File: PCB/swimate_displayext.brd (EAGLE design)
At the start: 50.9 x 51.2 mm, 56 parts, among them IC1 LPC11U24, T1 BSS84, T2 BSS84, U1 USD-SOCKETNEW, U3 NC7SV86P5X, U5 DS3231MZ/V+T, U6 MAX1595EUA33+, U7 MAX1811ESA-T, U8 MAX16054AZT+T, U9 HC_05, Y1 12.000MHz

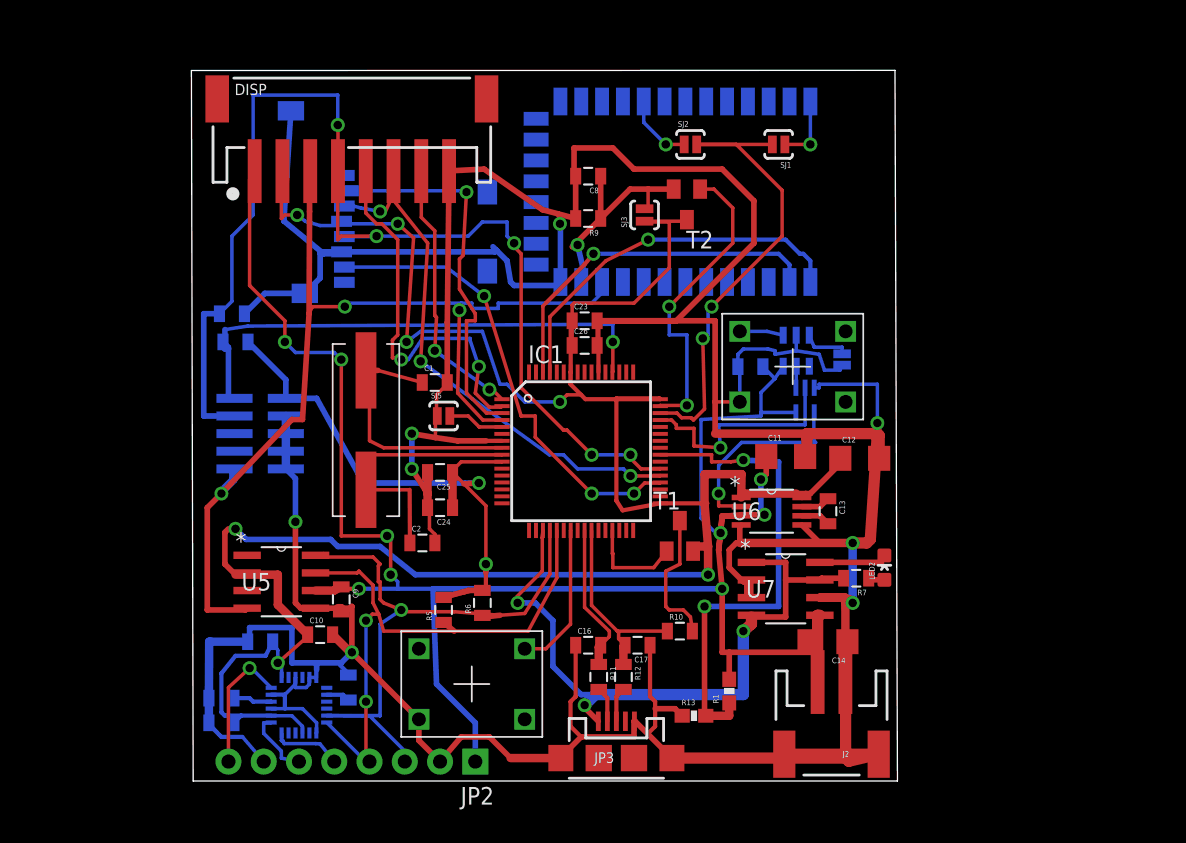
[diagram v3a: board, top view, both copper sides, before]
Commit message: Displayboard completed.. Need to check connector width
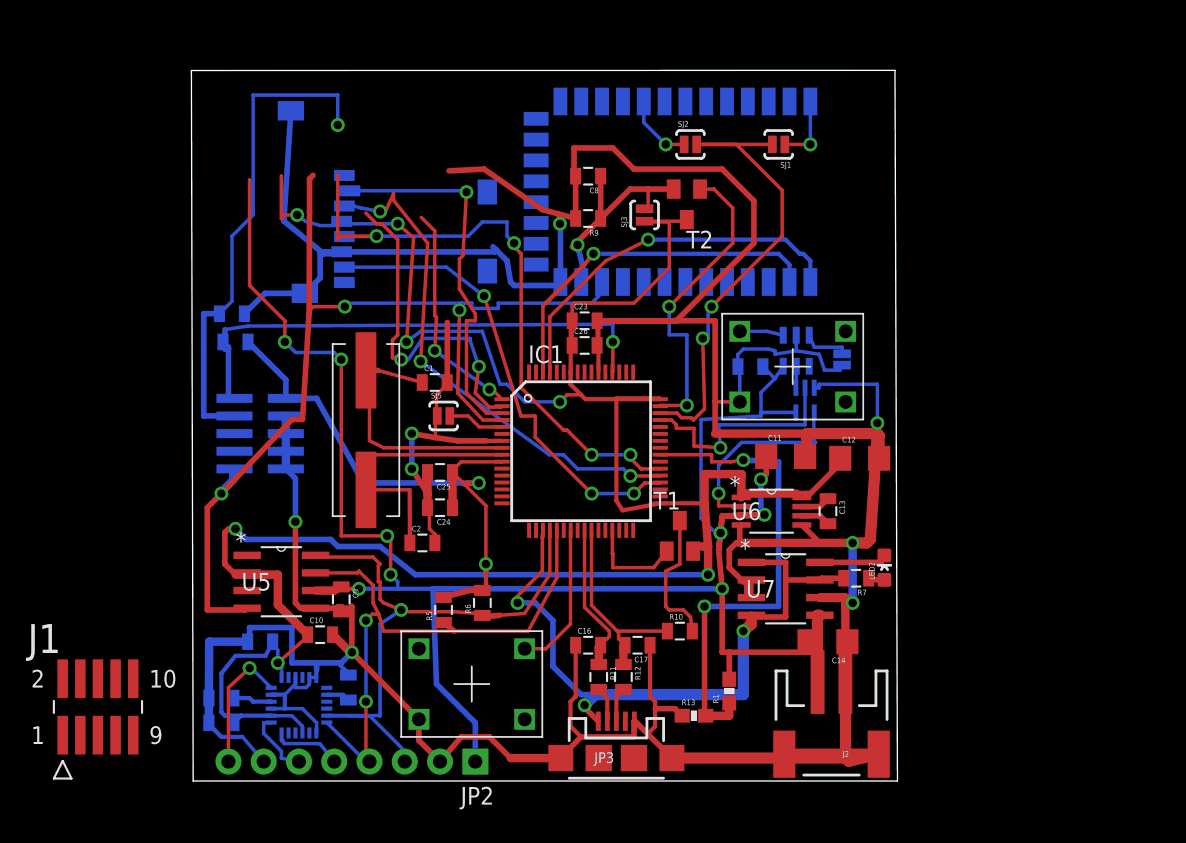
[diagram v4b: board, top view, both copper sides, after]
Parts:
- removed DISP: (no value), microbuilder:JSTPH8
- added J1: FTSH-105-01-L-DV, SAMTEC-HTSW-FTxx_By_element14_Batch_1:SAMTEC_FTSH-105-01-L-DV
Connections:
- net 3.3V: now also J1.2; no longer DISP.2
- net DISP_CS: now also J1.7; no longer DISP.5
- net DISP_DC: now also J1.1; no longer DISP.7
- net GND: now also J1.10, J1.6, J1.8; no longer DISP.8
- net RST: now also J1.3; no longer DISP.3
- net SPI0_MOSI: now also J1.9; no longer DISP.6
- net SPI0_SCK: now also J1.5; no longer DISP.4
- net VBAT: now also J1.4; no longer DISP.1
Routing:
- net GND: track 386.1 -> 375.2 mm
- net DISP_DC: track 19.4 -> 16.1 mm
- net SPI0_SCK: track 84.0 -> 80.8 mm
- net DISP_CS: track 27.7 -> 24.6 mm
- net SPI0_MOSI: track 39.2 -> 37.5 mm
- net VBAT: track 139.0 -> 138.3 mm
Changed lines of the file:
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@@
 <element name="R1" library="SparkFun-Passives" package="0603-RES" value="10k" x="38.608" y="6.096" rot="R90"/>
 <element name="R13" library="SparkFun-Passives" package="0603-RES" value="24k" x="36.068" y="4.318"/>
-<element name="DISP" library="microbuilder" package="JSTPH8" value="" x="11.43" y="47.244"/>
 <element name="SJ4" library="SparkFun-Passives" package="SJ_2S-NOTRACE" value="SOLDERJUMPERNC2" x="46.736" y="29.972" rot="MR90"/>
 <element name="U3" library="Fairchild_By_element14_Batch_1" package="SOT65P210X110-5N" value="NC7SV86P5X" x="44.069" y="27.051" rot="MR270">
@@
 <attribute name="SUPPLIER" value="Fairchild Semiconductor" x="44.069" y="27.051" size="1.778" layer="28" rot="MR270" display="off"/>
 <attribute name="OC_FARNELL" value="1467343" x="44.069" y="27.051" size="1.778" layer="28" rot="MR270" display="off"/>
+</element>
+<element name="J1" library="SAMTEC-HTSW-FTxx_By_element14_Batch_1" package="SAMTEC_FTSH-105-01-L-DV" value="FTSH-105-01-L-DV" x="-6.858" y="4.953">
+<attribute name="PACKAGE" value="HEADER, 1.27MM, 2X5WAY, SMT" x="-6.858" y="4.953" size="1.778" layer="27" display="off"/>
+<attribute name="OC_NEWARK" value="11P4814" x="-6.858" y="4.953" size="1.778" layer="27" display="off"/>
+<attribute name="MPN" value="FTSH-105-01-L-DV" x="-6.858" y="4.953" size="1.778" layer="27" display="off"/>
+<attribute name="SUPPLIER" value="SAMTEC" x="-6.858" y="4.953" size="1.778" layer="27" display="off"/>
+<attribute name="OC_FARNELL" value="1667759" x="-6.858" y="4.953" size="1.778" layer="27" display="off"/>
 </element>
 </elements>
@@
 <contactref element="U6" pad="3"/>
 <contactref element="R1" pad="2"/>
-<contactref element="DISP" pad="1"/>
 <wire x1="10.668" y1="13.6" x2="10.149" y2="13.335" width="0.6096" layer="1"/>
 <wire x1="10.149" y1="13.335" x2="8.8138" y2="13.335" width="0.6096" layer="1"/>
@@
 <wire x1="44.32" y1="9.652" x2="44.974" y2="8.89" width="0.3048" layer="1"/>
 <wire x1="38.608" y1="6.946" x2="38.608" y2="8.89" width="0.4064" layer="1"/>
-<wire x1="4.43" y1="43.544" x2="4.064" y2="42.924" width="0.254" layer="1"/>
 <wire x1="4.064" y1="42.924" x2="4.064" y2="35.306" width="0.254" layer="1"/>
 <wire x1="4.064" y1="35.306" x2="6.604" y2="32.766" width="0.254" layer="1"/>
@@
 <contactref element="U3" pad="5"/>
 <wire x1="43.4086" y1="26.162" x2="40.894" y2="26.162" width="0.254" layer="16"/>
+<contactref element="J1" pad="4"/>
+<wire x1="-8.128" y1="6.985" x2="8.8138" y2="13.335" width="0" layer="19" extent="1-1"/>
 </signal>
 <signal name="GND">
@@
 <contactref element="C17" pad="1"/>
 <contactref element="SW_MODE" pad="P$2"/>
-<contactref element="DISP" pad="8"/>
 <contactref element="U2" pad="1"/>
 <contactref element="U2" pad="11"/>
@@
 <wire x1="7.366" y1="21.408" x2="6.676" y2="22.098" width="0.4064" layer="16"/>
 <wire x1="18.299" y1="28.321" x2="18.303" y2="32.643" width="0.4064" layer="1"/>
-<wire x1="18.303" y1="32.643" x2="18.43" y2="43.544" width="0.4064" layer="1"/>
-<wire x1="18.43" y1="43.561" x2="18.43" y2="43.544" width="0.4064" layer="1"/>
 <wire x1="3.694" y1="33.274" x2="5.16" y2="34.74" width="0.4064" layer="16"/>
 <wire x1="5.16" y1="34.74" x2="8.04" y2="34.74" width="0.4064" layer="16"/>
@@
 <wire x1="26.416" y1="39.751" x2="26.416" y2="40.329078125" width="0.4064" layer="1"/>
 <wire x1="26.416" y1="40.329078125" x2="26.277096875" y2="40.46798125" width="0.4064" layer="1"/>
+<contactref element="J1" pad="6"/>
+<contactref element="J1" pad="8"/>
+<contactref element="J1" pad="10"/>
 <wire x1="29.094" y1="32.766" x2="28.956" y2="32.766" width="0" layer="19" extent="1-1"/>
+<wire x1="18.303" y1="32.643" x2="22.86" y2="35.56" width="0" layer="19" extent="1-16"/>
+<wire x1="-4.318" y1="6.985" x2="1.132" y2="5.588" width="0" layer="19" extent="1-16"/>
+<wire x1="-5.588" y1="6.985" x2="-4.318" y2="6.985" width="0" layer="19" extent="1-1"/>
+<wire x1="-6.858" y1="6.985" x2="-5.588" y2="6.985" width="0" layer="19" extent="1-1"/>
 </signal>
 <signal name="3.3V">
@@
 <contactref element="SJ3" pad="1"/>
 <contactref element="T1" pad="2"/>
-<contactref element="DISP" pad="2"/>
 <contactref element="U2" pad="3"/>
 <contactref element="U2" pad="13"/>
@@
 <wire x1="26.416" y1="26.924" x2="26.924" y2="27.432" width="0.254" layer="1"/>
 <wire x1="26.924" y1="27.432" x2="27.94" y2="27.432" width="0.254" layer="1"/>
-<wire x1="6.43" y1="43.544" x2="6.35" y2="43.21" width="0.254" layer="1"/>
 <wire x1="6.35" y1="43.21" x2="6.35" y2="40.132" width="0.254" layer="1"/>
 <wire x1="6.35" y1="40.132" x2="6.604" y2="40.386" width="0.254" layer="1"/>
@@
 <wire x1="6.37" y1="7.08" x2="6.37" y2="8.108" width="0.254" layer="16"/>
 <wire x1="6.37" y1="8.108" x2="6.096" y2="8.128" width="0.254" layer="16"/>
+<contactref element="J1" pad="2"/>
+<wire x1="-9.398" y1="6.985" x2="2.032" y2="7.366" width="0" layer="19" extent="1-16"/>
 </signal>
 <signal name="VUSB">
@@
 <contactref element="U1" pad="3"/>
 <contactref element="IC1" pad="37"/>
-<contactref element="DISP" pad="6"/>
-<wire x1="14.43" y1="43.544" x2="14.43" y2="41.91" width="0.254" layer="1"/>
 <wire x1="14.43" y1="41.91" x2="14.43" y2="41.45" width="0.254" layer="1"/>
 <wire x1="14.43" y1="41.45" x2="16.891" y2="38.354" width="0.254" layer="1"/>
@@
 <wire x1="13.462" y1="40.64" x2="13.795" y2="40.513" width="0.254" layer="1"/>
 <wire x1="13.795" y1="40.513" x2="14.43" y2="41.91" width="0.254" layer="1"/>
+<contactref element="J1" pad="9"/>
+<wire x1="-4.318" y1="2.921" x2="16.383" y2="29.845" width="0" layer="19" extent="1-1"/>
 </signal>
 <signal name="SPI0_SCK">
 <contactref element="U1" pad="5"/>
-<contactref element="DISP" pad="4"/>
 <contactref element="IC1" pad="38"/>
 <contactref element="JTAG1" pad="4"/>
@@
 <via x="10.414" y="46.863" extent="1-16" drill="0.6096"/>
 <wire x1="10.414" y1="46.863" x2="10.43" y2="46.466" width="0.254" layer="1"/>
-<wire x1="10.43" y1="46.466" x2="10.43" y2="43.544" width="0.254" layer="1"/>
-<wire x1="10.43" y1="43.544" x2="10.414" y2="43.274" width="0.254" layer="1"/>
 <wire x1="10.414" y1="43.274" x2="10.414" y2="38.608" width="0.254" layer="1"/>
 <wire x1="10.414" y1="38.608" x2="10.668" y2="38.862" width="0.254" layer="1"/>
@@
 <wire x1="32.258" y1="22.098" x2="33.62" y2="22.098" width="0.254" layer="1"/>
 <wire x1="33.62" y1="22.098" x2="33.64" y2="22.118" width="0.254" layer="1"/>
+<contactref element="J1" pad="5"/>
+<wire x1="10.43" y1="46.466" x2="10.414" y2="43.274" width="0" layer="19" extent="1-1"/>
+<wire x1="-6.858" y1="2.921" x2="0.762" y2="25.908" width="0" layer="19" extent="1-16"/>
 </signal>
 <signal name="SPI0_MISO">
@@
 <contactref element="JTAG1" pad="10"/>
 <contactref element="U9" pad="11"/>
-<contactref element="DISP" pad="3"/>
 <wire x1="3.8862" y1="12.065" x2="3.7592" y2="11.938" width="0.4064" layer="1"/>
 <wire x1="3.7592" y1="11.938" x2="1.016" y2="11.938" width="0.4064" layer="1"/>
@@
 <wire x1="2.032" y1="20.32" x2="7.112" y2="25.654" width="0.4064" layer="1"/>
 <wire x1="7.112" y1="25.654" x2="7.874" y2="25.654" width="0.4064" layer="1"/>
-<wire x1="8.43" y1="43.544" x2="8.636" y2="43.242" width="0.4064" layer="1"/>
 <wire x1="8.636" y1="43.242" x2="8.382" y2="42.988" width="0.4064" layer="1"/>
 <wire x1="8.382" y1="42.988" x2="8.382" y2="40.64" width="0.4064" layer="1"/>
@@
 <via x="19.177" y="33.528" extent="1-16" drill="0.6096"/>
 <wire x1="19.177" y1="33.528" x2="19.304" y2="34.036" width="0.254" layer="16"/>
+<contactref element="J1" pad="3"/>
+<wire x1="-8.128" y1="2.921" x2="1.016" y2="11.938" width="0" layer="19" extent="1-1"/>
 </signal>
 <signal name="MCU_RX">
@@
 </signal>
 <signal name="DISP_CS">
-<contactref element="DISP" pad="5"/>
 <contactref element="IC1" pad="2"/>
-<wire x1="12.43" y1="43.544" x2="12.43" y2="40.529" width="0.254" layer="1"/>
 <wire x1="12.43" y1="40.529" x2="13.208" y2="39.751" width="0.254" layer="1"/>
 <wire x1="13.208" y1="39.751" x2="13.589" y2="39.751" width="0.254" layer="1"/>
@@
 <wire x1="21.336" y1="26.543" x2="22.165" y2="26.543" width="0.254" layer="1"/>
 <wire x1="22.165" y1="26.543" x2="22.24" y2="26.618" width="0.254" layer="1"/>
+<contactref element="J1" pad="7"/>
+<wire x1="-5.588" y1="2.921" x2="14.351" y2="30.099" width="0" layer="19" extent="1-1"/>
 </signal>
 <signal name="DISP_DC">
-<contactref element="DISP" pad="7"/>
 <contactref element="IC1" pad="1"/>
-<wire x1="16.43" y1="43.544" x2="16.43" y2="40.212" width="0.254" layer="1"/>
 <wire x1="16.43" y1="40.212" x2="17.399" y2="39.243" width="0.254" layer="1"/>
 <wire x1="17.399" y1="39.243" x2="17.399" y2="33.147" width="0.254" layer="1"/>
@@
 <wire x1="21.336" y1="27.813" x2="21.672" y2="27.686" width="0.254" layer="1"/>
 <wire x1="21.672" y1="27.686" x2="22.24" y2="27.118" width="0.254" layer="1"/>
+<contactref element="J1" pad="1"/>
+<wire x1="-9.398" y1="2.921" x2="17.399" y2="30.607" width="0" layer="19" extent="1-1"/>
 </signal>
 <signal name="VBATMON">

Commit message: Moved connector onto page.
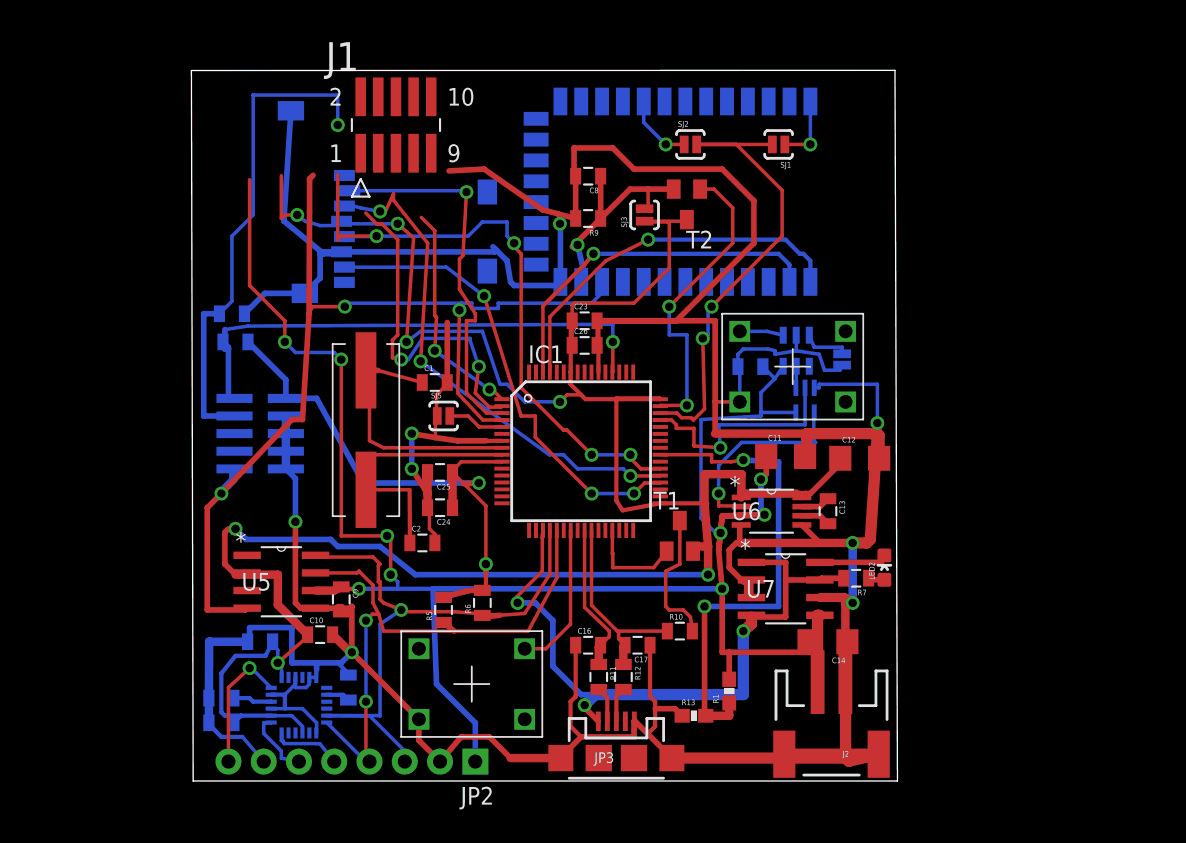
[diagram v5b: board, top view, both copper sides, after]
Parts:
- moved J1 47.1 mm to (14.6, 46.9)
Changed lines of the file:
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@@
 <?xml version="1.0" encoding="utf-8"?>
 <!DOCTYPE eagle SYSTEM "eagle.dtd">
-<eagle version="6.4">
+<eagle version="6.5.0">
 <drawing>
 <settings>
@@
 <attribute name="OC_FARNELL" value="1467343" x="44.069" y="27.051" size="1.778" layer="28" rot="MR270" display="off"/>
 </element>
-<element name="J1" library="SAMTEC-HTSW-FTxx_By_element14_Batch_1" package="SAMTEC_FTSH-105-01-L-DV" value="FTSH-105-01-L-DV" x="-6.858" y="4.953">
-<attribute name="PACKAGE" value="HEADER, 1.27MM, 2X5WAY, SMT" x="-6.858" y="4.953" size="1.778" layer="27" display="off"/>
-<attribute name="OC_NEWARK" value="11P4814" x="-6.858" y="4.953" size="1.778" layer="27" display="off"/>
-<attribute name="MPN" value="FTSH-105-01-L-DV" x="-6.858" y="4.953" size="1.778" layer="27" display="off"/>
-<attribute name="SUPPLIER" value="SAMTEC" x="-6.858" y="4.953" size="1.778" layer="27" display="off"/>
-<attribute name="OC_FARNELL" value="1667759" x="-6.858" y="4.953" size="1.778" layer="27" display="off"/>
+<element name="J1" library="SAMTEC-HTSW-FTxx_By_element14_Batch_1" package="SAMTEC_FTSH-105-01-L-DV" value="FTSH-105-01-L-DV" x="14.605" y="46.863">
+<attribute name="PACKAGE" value="HEADER, 1.27MM, 2X5WAY, SMT" x="14.605" y="46.863" size="1.778" layer="27" display="off"/>
+<attribute name="OC_NEWARK" value="11P4814" x="14.605" y="46.863" size="1.778" layer="27" display="off"/>
+<attribute name="MPN" value="FTSH-105-01-L-DV" x="14.605" y="46.863" size="1.778" layer="27" display="off"/>
+<attribute name="SUPPLIER" value="SAMTEC" x="14.605" y="46.863" size="1.778" layer="27" display="off"/>
+<attribute name="OC_FARNELL" value="1667759" x="14.605" y="46.863" size="1.778" layer="27" display="off"/>
 </element>
 </elements>
@@
 <wire x1="43.4086" y1="26.162" x2="40.894" y2="26.162" width="0.254" layer="16"/>
 <contactref element="J1" pad="4"/>
-<wire x1="-8.128" y1="6.985" x2="8.8138" y2="13.335" width="0" layer="19" extent="1-1"/>
+<wire x1="13.335" y1="48.895" x2="8.8138" y2="13.335" width="0" layer="19" extent="1-1"/>
 </signal>
 <signal name="GND">
@@
 <wire x1="29.094" y1="32.766" x2="28.956" y2="32.766" width="0" layer="19" extent="1-1"/>
 <wire x1="18.303" y1="32.643" x2="22.86" y2="35.56" width="0" layer="19" extent="1-16"/>
-<wire x1="-4.318" y1="6.985" x2="1.132" y2="5.588" width="0" layer="19" extent="1-16"/>
-<wire x1="-5.588" y1="6.985" x2="-4.318" y2="6.985" width="0" layer="19" extent="1-1"/>
-<wire x1="-6.858" y1="6.985" x2="-5.588" y2="6.985" width="0" layer="19" extent="1-1"/>
+<wire x1="17.145" y1="48.895" x2="1.132" y2="5.588" width="0" layer="19" extent="1-16"/>
+<wire x1="15.875" y1="48.895" x2="17.145" y2="48.895" width="0" layer="19" extent="1-1"/>
+<wire x1="14.605" y1="48.895" x2="15.875" y2="48.895" width="0" layer="19" extent="1-1"/>
 </signal>
 <signal name="3.3V">
@@
 <wire x1="6.37" y1="8.108" x2="6.096" y2="8.128" width="0.254" layer="16"/>
 <contactref element="J1" pad="2"/>
-<wire x1="-9.398" y1="6.985" x2="2.032" y2="7.366" width="0" layer="19" extent="1-16"/>
+<wire x1="12.065" y1="48.895" x2="2.032" y2="7.366" width="0" layer="19" extent="1-16"/>
 </signal>
 <signal name="VUSB">
@@
 <wire x1="13.795" y1="40.513" x2="14.43" y2="41.91" width="0.254" layer="1"/>
 <contactref element="J1" pad="9"/>
-<wire x1="-4.318" y1="2.921" x2="16.383" y2="29.845" width="0" layer="19" extent="1-1"/>
+<wire x1="17.145" y1="44.831" x2="16.383" y2="29.845" width="0" layer="19" extent="1-1"/>
 </signal>
 <signal name="SPI0_SCK">
@@
 <contactref element="J1" pad="5"/>
 <wire x1="10.43" y1="46.466" x2="10.414" y2="43.274" width="0" layer="19" extent="1-1"/>
-<wire x1="-6.858" y1="2.921" x2="0.762" y2="25.908" width="0" layer="19" extent="1-16"/>
+<wire x1="14.605" y1="44.831" x2="0.762" y2="25.908" width="0" layer="19" extent="1-16"/>
 </signal>
 <signal name="SPI0_MISO">
@@
 <wire x1="19.177" y1="33.528" x2="19.304" y2="34.036" width="0.254" layer="16"/>
 <contactref element="J1" pad="3"/>
-<wire x1="-8.128" y1="2.921" x2="1.016" y2="11.938" width="0" layer="19" extent="1-1"/>
+<wire x1="13.335" y1="44.831" x2="1.016" y2="11.938" width="0" layer="19" extent="1-1"/>
 </signal>
 <signal name="MCU_RX">
@@
 <wire x1="22.165" y1="26.543" x2="22.24" y2="26.618" width="0.254" layer="1"/>
 <contactref element="J1" pad="7"/>
-<wire x1="-5.588" y1="2.921" x2="14.351" y2="30.099" width="0" layer="19" extent="1-1"/>
+<wire x1="15.875" y1="44.831" x2="14.351" y2="30.099" width="0" layer="19" extent="1-1"/>
 </signal>
 <signal name="DISP_DC">
@@
 <wire x1="21.672" y1="27.686" x2="22.24" y2="27.118" width="0.254" layer="1"/>
 <contactref element="J1" pad="1"/>
-<wire x1="-9.398" y1="2.921" x2="17.399" y2="30.607" width="0" layer="19" extent="1-1"/>
+<wire x1="12.065" y1="44.831" x2="17.399" y2="30.607" width="0" layer="19" extent="1-1"/>
 </signal>
 <signal name="VBATMON">
